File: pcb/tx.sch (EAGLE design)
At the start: 54 parts, among them U3 MCP73831T-2ACI/OT, Y1 CRYSTAL-26MHZSMD-3.2X2.5

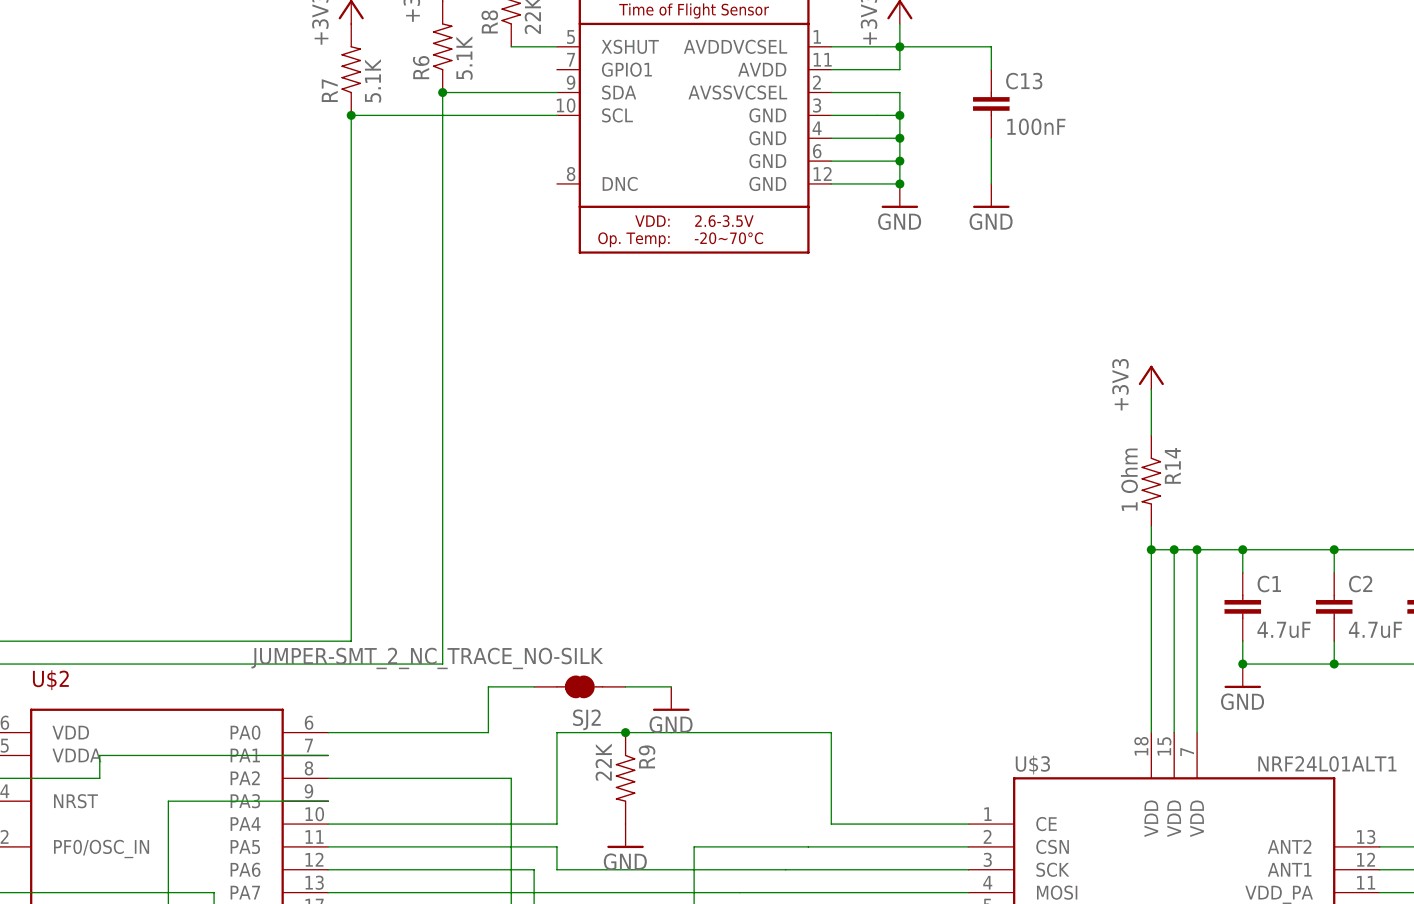
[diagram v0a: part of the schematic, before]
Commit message: tx added mosfet switch
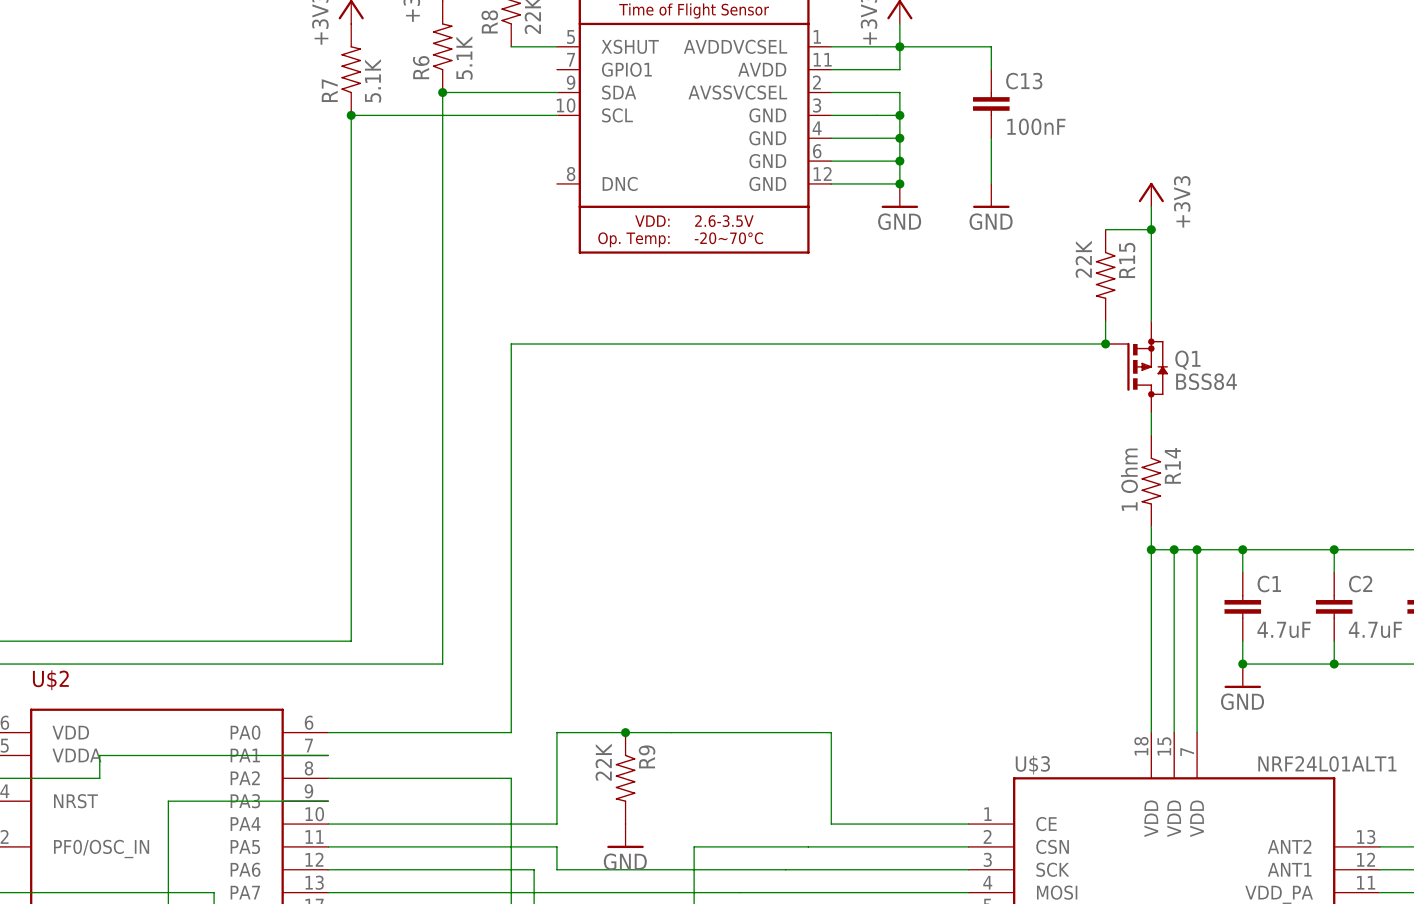
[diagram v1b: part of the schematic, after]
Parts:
- removed SJ2: JUMPER-SMT_2_NC_TRACE_NO-SILK, SparkFun-Jumpers:JUMPER-SMT_2_NC_TRACE_NO-SILK
- added Q1: BSS84, transistor-small-signal:BSS84
- added R15: 22K, joyAnalog:RESISTOR0805-RES
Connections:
- removed net N$36: SJ2.2, U$2.PA0
- new net N$38: Q1.D, R14.1
- new net N$39: Q1.G, R15.2, U$2.PA0
- net +3V3: now also Q1.S, R15.1; no longer R14.1
- net GND: no longer SJ2.1
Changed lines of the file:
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@@
 <part name="JP1" library="adafruit_changed" deviceset="PINHD-1X3" device="CB"/>
 <part name="+3V8" library="supply1" library_urn="urn:adsk.eagle:library:371" deviceset="+3V3" device=""/>
-<part name="SJ2" library="SparkFun-Jumpers" deviceset="JUMPER-SMT_2_NC_TRACE" device="_NO-SILK"/>
 <part name="U$4" library="my_usbc_16p" deviceset="USBC_16P" device=""/>
 <part name="R13" library="joyAnalog" deviceset="RESISTOR" device="0805-RES" value="22K"/>
@@
 <part name="E1" library="esp32-thing-temp" deviceset="ANTENNA" device="TRACE-TUNED" value="ANTENNA"/>
 <part name="GND18" library="clock" deviceset="GND" device=""/>
-<part name="GND27" library="supply1" library_urn="urn:adsk.eagle:library:371" deviceset="GND" device=""/>
 <part name="U$1" library="3pos_slide_switch" deviceset="M2_SCREW_DEV" device=""/>
 <part name="U$12" library="3pos_slide_switch" deviceset="M2_SCREW_DEV" device=""/>
@@
 <part name="U$14" library="3pos_slide_switch" deviceset="M2_SCREW_DEV" device=""/>
 <part name="R14" library="joyAnalog" deviceset="RESISTOR" device="0805-RES" value="1 Ohm"/>
+<part name="Q1" library="transistor-small-signal" deviceset="BSS84" device=""/>
+<part name="R15" library="joyAnalog" deviceset="RESISTOR" device="0805-RES" value="22K"/>
 </parts>
 <sheets>
@@
 </instance>
 <instance part="U$3" gate="G$1" x="99.06" y="-60.96"/>
-<instance part="+3V1" gate="G$1" x="96.52" y="-2.54"/>
+<instance part="+3V1" gate="G$1" x="96.52" y="17.78" rot="MR0"/>
 <instance part="GND1" gate="1" x="88.9" y="-91.44"/>
 <instance part="C1" gate="G$1" x="106.68" y="-30.48"/>
@@
 <instance part="JP1" gate="A" x="22.86" y="-91.44" rot="R270"/>
 <instance part="+3V8" gate="G$1" x="25.4" y="45.72"/>
-<instance part="SJ2" gate="G$1" x="33.02" y="-38.1" rot="R180"/>
 <instance part="U$4" gate="G$1" x="-254" y="-27.94"/>
 <instance part="R13" gate="G$1" x="-33.02" y="-119.38" rot="R270"/>
@@
 <instance part="E1" gate="G$1" x="218.44" y="-55.88" rot="R270"/>
 <instance part="GND18" gate="1" x="200.66" y="-60.96"/>
-<instance part="GND27" gate="1" x="43.18" y="-40.64"/>
 <instance part="U$1" gate="G$1" x="-137.16" y="-144.78"/>
 <instance part="U$12" gate="G$1" x="-93.98" y="-147.32"/>
@@
 <instance part="U$14" gate="G$1" x="-157.48" y="-170.18"/>
 <instance part="R14" gate="G$1" x="96.52" y="-15.24" rot="R270"/>
+<instance part="Q1" gate="G$1" x="96.52" y="-2.54"/>
+<instance part="R15" gate="G$1" x="91.44" y="7.62" rot="R270"/>
 </instances>
 <busses>
@@
 <wire x1="200.66" y1="-58.42" x2="208.28" y2="-58.42" width="0.1524" layer="91"/>
 </segment>
-<segment>
-<pinref part="SJ2" gate="G$1" pin="1"/>
-<wire x1="43.18" y1="-38.1" x2="38.1" y2="-38.1" width="0.1524" layer="91"/>
-<pinref part="GND27" gate="1" pin="GND"/>
-</segment>
 </net>
 <net name="+3V3" class="0">
@@
 </segment>
 <segment>
+<pinref part="Q1" gate="G$1" pin="S"/>
 <pinref part="+3V1" gate="G$1" pin="+3V3"/>
-<pinref part="R14" gate="G$1" pin="1"/>
-<wire x1="96.52" y1="-5.08" x2="96.52" y2="-10.16" width="0.1524" layer="91"/>
+<wire x1="96.52" y1="15.24" x2="96.52" y2="12.7" width="0.1524" layer="91"/>
+<pinref part="R15" gate="G$1" pin="1"/>
+<wire x1="96.52" y1="12.7" x2="96.52" y2="2.54" width="0.1524" layer="91"/>
+<wire x1="91.44" y1="12.7" x2="96.52" y2="12.7" width="0.1524" layer="91"/>
+<junction x="96.52" y="12.7"/>
 </segment>
 </net>
@@
 </segment>
 </net>
-<net name="N$36" class="0">
-<segment>
-<pinref part="U$2" gate="G$1" pin="PA0"/>
-<wire x1="5.08" y1="-43.18" x2="22.86" y2="-43.18" width="0.1524" layer="91"/>
-<wire x1="22.86" y1="-43.18" x2="22.86" y2="-38.1" width="0.1524" layer="91"/>
-<pinref part="SJ2" gate="G$1" pin="2"/>
-<wire x1="22.86" y1="-38.1" x2="27.94" y2="-38.1" width="0.1524" layer="91"/>
-</segment>
-</net>
 <net name="N$37" class="0">
 <segment>
@@
 </segment>
 </net>
+<net name="N$38" class="0">
+<segment>
+<pinref part="R14" gate="G$1" pin="1"/>
+<pinref part="Q1" gate="G$1" pin="D"/>
+<wire x1="96.52" y1="-7.62" x2="96.52" y2="-10.16" width="0.1524" layer="91"/>
+</segment>
+</net>
+<net name="N$39" class="0">
+<segment>
+<pinref part="R15" gate="G$1" pin="2"/>
+<pinref part="Q1" gate="G$1" pin="G"/>
+<wire x1="91.44" y1="2.54" x2="91.44" y2="0" width="0.1524" layer="91"/>
+<pinref part="U$2" gate="G$1" pin="PA0"/>
+<wire x1="5.08" y1="-43.18" x2="25.4" y2="-43.18" width="0.1524" layer="91"/>
+<wire x1="25.4" y1="-43.18" x2="25.4" y2="0" width="0.1524" layer="91"/>
+<wire x1="25.4" y1="0" x2="91.44" y2="0" width="0.1524" layer="91"/>
+<junction x="91.44" y="0"/>
+</segment>
+</net>

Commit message: before trail run
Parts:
- C8, C9: value 22pF -> 12pF
- Y1: value CRYSTAL-26MHZSMD-3.2X2.5 -> 16MHz_12pF
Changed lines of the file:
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@@
 <part name="GND5" library="clock" deviceset="GND" device=""/>
 <part name="GND8" library="clock" deviceset="GND" device=""/>
-<part name="C8" library="clock" deviceset="CAP" device="0805" value="22pF"/>
+<part name="C8" library="clock" deviceset="CAP" device="0805" value="12pF"/>
 <part name="GND10" library="clock" deviceset="GND" device=""/>
-<part name="C9" library="clock" deviceset="CAP" device="0805" value="22pF"/>
+<part name="C9" library="clock" deviceset="CAP" device="0805" value="12pF"/>
 <part name="GND11" library="clock" deviceset="GND" device=""/>
-<part name="Y1" library="SparkFun-Clocks" deviceset="CRYSTAL-26MHZ" device="SMD-3.2X2.5"/>
+<part name="Y1" library="SparkFun-Clocks" deviceset="CRYSTAL-26MHZ" device="SMD-3.2X2.5" value="16MHz_12pF"/>
 <part name="GND6" library="supply1" deviceset="GND" device=""/>
 <part name="R3" library="joyAnalog" deviceset="RESISTOR" device="0805-RES" value="5.1K"/>

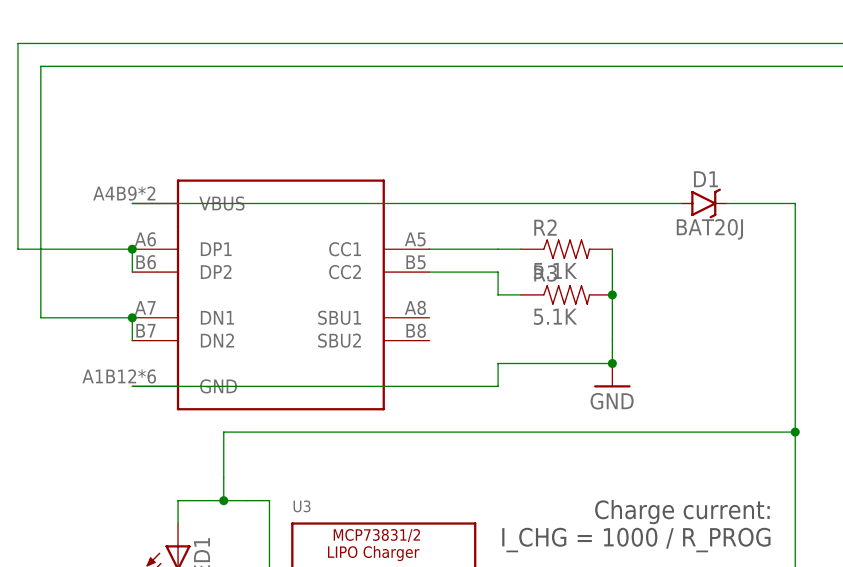
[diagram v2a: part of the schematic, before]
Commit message: centered usbc footprint, adjusted board layout
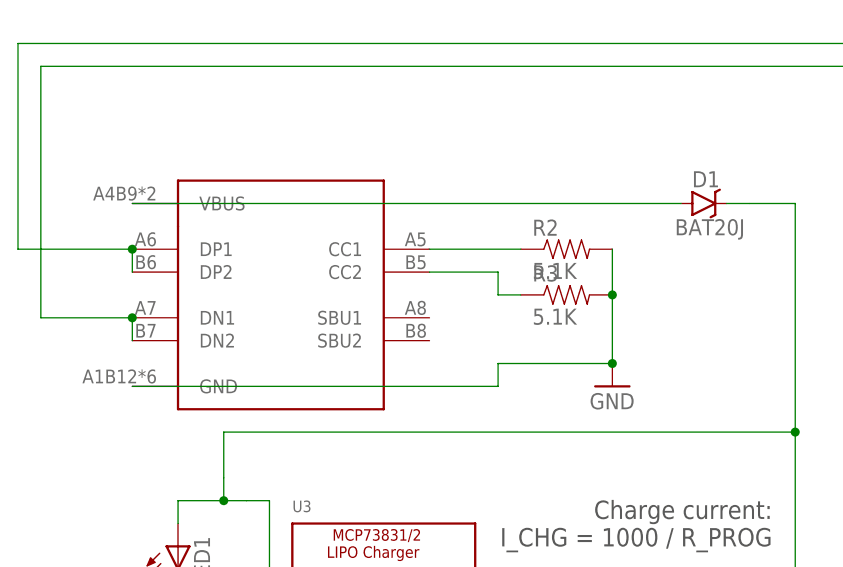
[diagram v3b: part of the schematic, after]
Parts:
- removed U$4: USBC_16P, my_usbc_16p:USBC_16P
- added U$5: USBC_16P_CENTERED, my_usbc_16p_centered:USBC_16P_CENTERED
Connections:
- net GND: now also U$5.GND; no longer U$4.GND
- net N$10: now also U$5.CC2; no longer U$4.CC2
- net N$11: now also U$5.CC1; no longer U$4.CC1
- net N$18: now also U$5.DP1, U$5.DP2; no longer U$4.DP1, U$4.DP2
- net N$26: now also U$5.VBUS; no longer U$4.VBUS
- net N$34: now also U$5.DN1, U$5.DN2; no longer U$4.DN1, U$4.DN2
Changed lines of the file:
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@@
 <part name="JP1" library="adafruit_changed" deviceset="PINHD-1X3" device="CB"/>
 <part name="+3V8" library="supply1" library_urn="urn:adsk.eagle:library:371" deviceset="+3V3" device=""/>
-<part name="U$4" library="my_usbc_16p" deviceset="USBC_16P" device=""/>
 <part name="R13" library="joyAnalog" deviceset="RESISTOR" device="0805-RES" value="22K"/>
 <part name="GND26" library="supply1" library_urn="urn:adsk.eagle:library:371" deviceset="GND" device=""/>
@@
 <part name="Q1" library="transistor-small-signal" deviceset="BSS84" device=""/>
 <part name="R15" library="joyAnalog" deviceset="RESISTOR" device="0805-RES" value="22K"/>
+<part name="U$5" library="my_usbc_16p_centered" deviceset="USBC_16P_CENTERED" device=""/>
 </parts>
 <sheets>
@@
 <instance part="JP1" gate="A" x="22.86" y="-91.44" rot="R270"/>
 <instance part="+3V8" gate="G$1" x="25.4" y="45.72"/>
-<instance part="U$4" gate="G$1" x="-254" y="-27.94"/>
 <instance part="R13" gate="G$1" x="-33.02" y="-119.38" rot="R270"/>
 <instance part="GND26" gate="1" x="-33.02" y="-127"/>
@@
 <instance part="Q1" gate="G$1" x="96.52" y="-2.54"/>
 <instance part="R15" gate="G$1" x="91.44" y="7.62" rot="R270"/>
+<instance part="U$5" gate="G$1" x="-254" y="-27.94"/>
 </instances>
 <busses>
@@
 <segment>
 <pinref part="GND6" gate="1" pin="GND"/>
-<wire x1="-215.9" y1="-22.86" x2="-215.9" y2="-25.4" width="0.1524" layer="91"/>
 <pinref part="R3" gate="G$1" pin="2"/>
-<wire x1="-215.9" y1="-17.78" x2="-215.9" y2="-22.86" width="0.1524" layer="91"/>
+<wire x1="-215.9" y1="-17.78" x2="-215.9" y2="-25.4" width="0.1524" layer="91"/>
 <pinref part="R2" gate="G$1" pin="2"/>
 <wire x1="-215.9" y1="-12.7" x2="-215.9" y2="-17.78" width="0.1524" layer="91"/>
 <junction x="-215.9" y="-17.78"/>
-<pinref part="U$4" gate="G$1" pin="GND"/>
 <wire x1="-269.24" y1="-27.94" x2="-228.6" y2="-27.94" width="0.1524" layer="91"/>
 <wire x1="-228.6" y1="-27.94" x2="-228.6" y2="-25.4" width="0.1524" layer="91"/>
 <wire x1="-228.6" y1="-25.4" x2="-215.9" y2="-25.4" width="0.1524" layer="91"/>
 <junction x="-215.9" y="-25.4"/>
+<pinref part="U$5" gate="G$1" pin="GND"/>
 </segment>
 <segment>
@@
 <pinref part="R3" gate="G$1" pin="1"/>
 <wire x1="-228.6" y1="-17.78" x2="-226.06" y2="-17.78" width="0.1524" layer="91"/>
-<pinref part="U$4" gate="G$1" pin="CC2"/>
 <wire x1="-236.22" y1="-15.24" x2="-228.6" y2="-15.24" width="0.1524" layer="91"/>
 <wire x1="-228.6" y1="-15.24" x2="-228.6" y2="-17.78" width="0.1524" layer="91"/>
+<pinref part="U$5" gate="G$1" pin="CC2"/>
 </segment>
 </net>
@@
 <segment>
 <pinref part="R2" gate="G$1" pin="1"/>
-<wire x1="-228.6" y1="-12.7" x2="-226.06" y2="-12.7" width="0.1524" layer="91"/>
-<pinref part="U$4" gate="G$1" pin="CC1"/>
-<wire x1="-236.22" y1="-12.7" x2="-228.6" y2="-12.7" width="0.1524" layer="91"/>
+<wire x1="-236.22" y1="-12.7" x2="-226.06" y2="-12.7" width="0.1524" layer="91"/>
+<pinref part="U$5" gate="G$1" pin="CC1"/>
 </segment>
 </net>
@@
 <net name="N$26" class="0">
 <segment>
-<wire x1="-228.6" y1="-7.62" x2="-210.82" y2="-7.62" width="0.1524" layer="91"/>
 <pinref part="D1" gate="G$1" pin="A"/>
-<wire x1="-210.82" y1="-7.62" x2="-208.28" y2="-7.62" width="0.1524" layer="91"/>
-<pinref part="U$4" gate="G$1" pin="VBUS"/>
-<wire x1="-269.24" y1="-7.62" x2="-231.14" y2="-7.62" width="0.1524" layer="91"/>
-<wire x1="-231.14" y1="-7.62" x2="-228.6" y2="-7.62" width="0.1524" layer="91"/>
+<wire x1="-269.24" y1="-7.62" x2="-208.28" y2="-7.62" width="0.1524" layer="91"/>
+<pinref part="U$5" gate="G$1" pin="VBUS"/>
 </segment>
 </net>
@@
 <net name="N$18" class="0">
 <segment>
-<pinref part="U$4" gate="G$1" pin="DP1"/>
-<pinref part="U$4" gate="G$1" pin="DP2"/>
 <wire x1="-269.24" y1="-12.7" x2="-269.24" y2="-15.24" width="0.1524" layer="91"/>
 <pinref part="U$2" gate="G$1" pin="PA10"/>
@@
 <wire x1="-281.94" y1="10.16" x2="-281.94" y2="-12.7" width="0.1524" layer="91"/>
 <wire x1="-281.94" y1="-12.7" x2="-269.24" y2="-12.7" width="0.1524" layer="91"/>
+<pinref part="U$5" gate="G$1" pin="DP1"/>
 <junction x="-269.24" y="-12.7"/>
+<pinref part="U$5" gate="G$1" pin="DP2"/>
 </segment>
 </net>
 <net name="N$34" class="0">
 <segment>
-<pinref part="U$4" gate="G$1" pin="DN1"/>
-<pinref part="U$4" gate="G$1" pin="DN2"/>
 <wire x1="-269.24" y1="-20.32" x2="-269.24" y2="-22.86" width="0.1524" layer="91"/>
 <pinref part="U$2" gate="G$1" pin="PA9"/>
@@
 <wire x1="-279.4" y1="7.62" x2="-279.4" y2="-20.32" width="0.1524" layer="91"/>
 <wire x1="-279.4" y1="-20.32" x2="-269.24" y2="-20.32" width="0.1524" layer="91"/>
+<pinref part="U$5" gate="G$1" pin="DN1"/>
 <junction x="-269.24" y="-20.32"/>
-</segment>
-</net>
+<pinref part="U$5" gate="G$1" pin="DN2"/>
+</segment>
+</net>

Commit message: foodprint adjustment, coord file
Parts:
- renumbered S2 to SW1, U$10 to SW2, U$2 to IC1, U$3 to IC2, U$5 to U2, U$9 to U4

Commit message: updated USBC connector, check_battery DBZ
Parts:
- U2: value USBC_16P_CENTERED -> USBC_16P; device my_usbc_16p_centered:USBC_16P_CENTERED -> my_usbc_16p:USBC_16P
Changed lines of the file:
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@@
 <part name="Q1" library="transistor-small-signal" deviceset="BSS84" device=""/>
 <part name="R15" library="joyAnalog" deviceset="RESISTOR" device="0805-RES" value="22K"/>
-<part name="U2" library="my_usbc_16p_centered" deviceset="USBC_16P_CENTERED" device=""/>
+<part name="U2" library="my_usbc_16p" deviceset="USBC_16P" device=""/>
 </parts>
 <sheets>
